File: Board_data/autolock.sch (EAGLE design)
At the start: 10 parts, among them CN1 RASPBERRYPI-GPIO

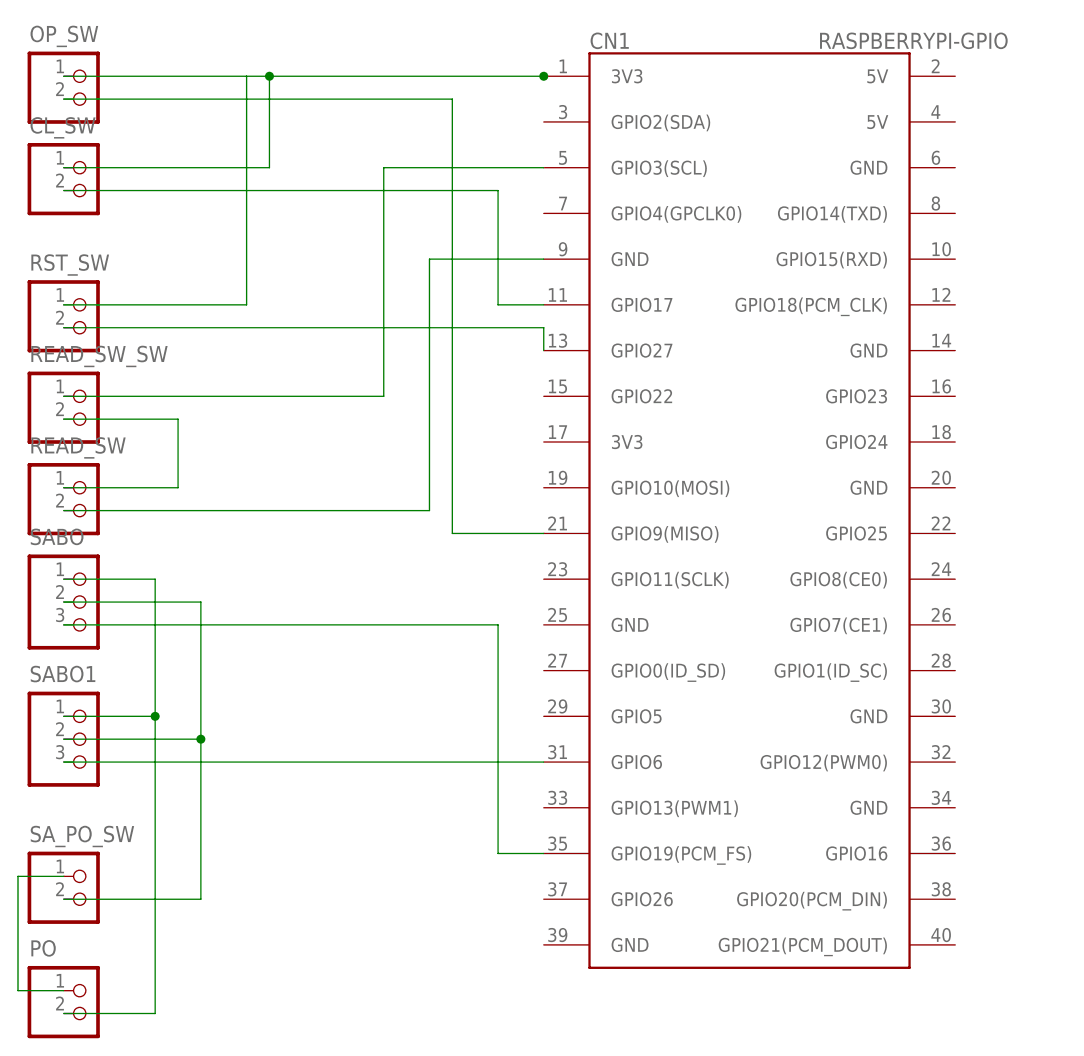
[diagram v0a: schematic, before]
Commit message: 基板修正・リードスイッチ調整
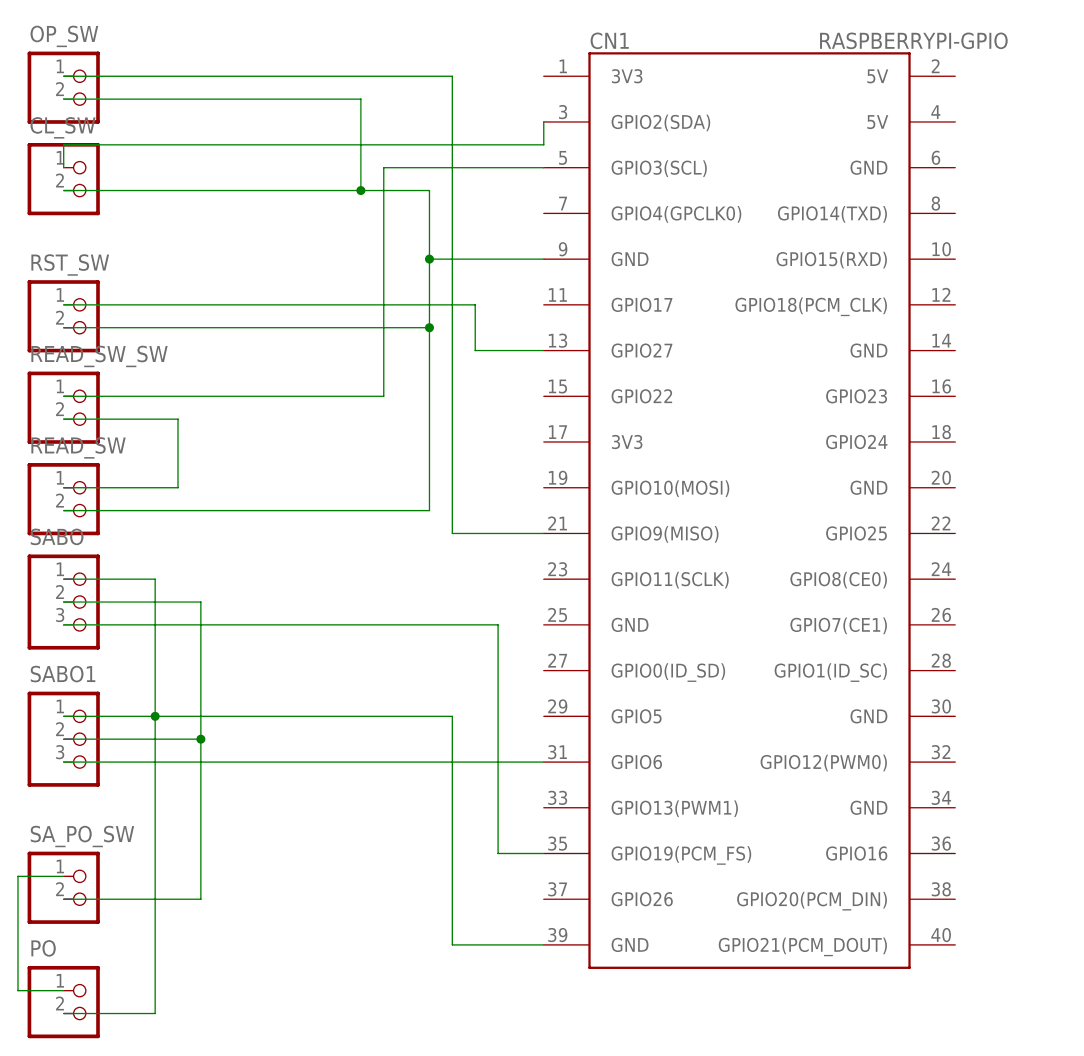
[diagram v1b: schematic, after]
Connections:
- removed net N$12: PO.2, SABO.1, SABO1.1
- removed net N$4: CN1.GND@2, READ_SW.2
- removed net N$8: CL_SW.2, CN1.GPIO17
- removed net N$9: CN1.GPIO27, RST_SW.2
- new net GND: CL_SW.2, CN1.GND@2, CN1.GND@8, OP_SW.2, PO.2, READ_SW.2, RST_SW.2, SABO.1, SABO1.1
- new net N$14: CN1.GPIO27, RST_SW.1
- net N$1: now also CN1.GPIO9(MISO); no longer CL_SW.1, CN1.3V3@1, RST_SW.1
- net N$2: now also CL_SW.1, CN1.GPIO2(SDA); no longer CN1.GPIO9(MISO), OP_SW.2
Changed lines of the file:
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@@
 <segment>
 <pinref part="OP_SW" gate="G$1" pin="1"/>
-<pinref part="CN1" gate="G$1" pin="3V3@1"/>
-<wire x1="30.48" y1="93.98" x2="50.8" y2="93.98" width="0.1524" layer="91"/>
-<pinref part="RST_SW" gate="G$1" pin="1"/>
-<wire x1="30.48" y1="68.58" x2="50.8" y2="68.58" width="0.1524" layer="91"/>
-<wire x1="50.8" y1="68.58" x2="50.8" y2="93.98" width="0.1524" layer="91"/>
-<wire x1="50.8" y1="93.98" x2="53.34" y2="93.98" width="0.1524" layer="91"/>
-<junction x="83.82" y="93.98"/>
-<pinref part="CL_SW" gate="G$1" pin="1"/>
-<wire x1="53.34" y1="93.98" x2="83.82" y2="93.98" width="0.1524" layer="91"/>
-<wire x1="30.48" y1="83.82" x2="53.34" y2="83.82" width="0.1524" layer="91"/>
-<wire x1="53.34" y1="83.82" x2="53.34" y2="93.98" width="0.1524" layer="91"/>
-<junction x="53.34" y="93.98"/>
-</segment>
-</net>
-<net name="N$2" class="0">
-<segment>
-<pinref part="OP_SW" gate="G$1" pin="2"/>
-<wire x1="30.48" y1="91.44" x2="73.66" y2="91.44" width="0.1524" layer="91"/>
-<wire x1="73.66" y1="91.44" x2="73.66" y2="43.18" width="0.1524" layer="91"/>
+<wire x1="30.48" y1="93.98" x2="73.66" y2="93.98" width="0.1524" layer="91"/>
+<wire x1="73.66" y1="93.98" x2="73.66" y2="43.18" width="0.1524" layer="91"/>
 <pinref part="CN1" gate="G$1" pin="GPIO9(MISO)"/>
 <wire x1="73.66" y1="43.18" x2="83.82" y2="43.18" width="0.1524" layer="91"/>
@@
 </segment>
 </net>
-<net name="N$4" class="0">
+<net name="GND" class="0">
 <segment>
-<wire x1="71.12" y1="45.72" x2="71.12" y2="73.66" width="0.1524" layer="91"/>
+<wire x1="71.12" y1="45.72" x2="71.12" y2="66.04" width="0.1524" layer="91"/>
 <pinref part="CN1" gate="G$1" pin="GND@2"/>
+<wire x1="71.12" y1="66.04" x2="71.12" y2="73.66" width="0.1524" layer="91"/>
 <wire x1="71.12" y1="73.66" x2="83.82" y2="73.66" width="0.1524" layer="91"/>
 <pinref part="READ_SW" gate="G$1" pin="2"/>
 <wire x1="30.48" y1="45.72" x2="71.12" y2="45.72" width="0.1524" layer="91"/>
+<pinref part="CL_SW" gate="G$1" pin="2"/>
+<wire x1="30.48" y1="81.28" x2="63.5" y2="81.28" width="0.1524" layer="91"/>
+<wire x1="63.5" y1="81.28" x2="71.12" y2="81.28" width="0.1524" layer="91"/>
+<wire x1="71.12" y1="81.28" x2="71.12" y2="73.66" width="0.1524" layer="91"/>
+<junction x="71.12" y="73.66"/>
+<pinref part="OP_SW" gate="G$1" pin="2"/>
+<wire x1="30.48" y1="91.44" x2="63.5" y2="91.44" width="0.1524" layer="91"/>
+<wire x1="63.5" y1="91.44" x2="63.5" y2="81.28" width="0.1524" layer="91"/>
+<junction x="63.5" y="81.28"/>
+<pinref part="RST_SW" gate="G$1" pin="2"/>
+<wire x1="30.48" y1="66.04" x2="71.12" y2="66.04" width="0.1524" layer="91"/>
+<junction x="71.12" y="66.04"/>
+</segment>
+<segment>
+<pinref part="SABO" gate="G$1" pin="1"/>
+<wire x1="30.48" y1="38.1" x2="40.64" y2="38.1" width="0.1524" layer="91"/>
+<wire x1="40.64" y1="38.1" x2="40.64" y2="22.86" width="0.1524" layer="91"/>
+<wire x1="40.64" y1="22.86" x2="40.64" y2="-10.16" width="0.1524" layer="91"/>
+<pinref part="SABO1" gate="G$1" pin="1"/>
+<wire x1="30.48" y1="22.86" x2="40.64" y2="22.86" width="0.1524" layer="91"/>
+<junction x="40.64" y="22.86"/>
+<wire x1="30.48" y1="-10.16" x2="40.64" y2="-10.16" width="0.1524" layer="91"/>
+<pinref part="PO" gate="G$1" pin="2"/>
+<wire x1="40.64" y1="22.86" x2="73.66" y2="22.86" width="0.1524" layer="91"/>
+<pinref part="CN1" gate="G$1" pin="GND@8"/>
+<wire x1="73.66" y1="-2.54" x2="83.82" y2="-2.54" width="0.1524" layer="91"/>
+<wire x1="73.66" y1="22.86" x2="73.66" y2="-2.54" width="0.1524" layer="91"/>
 </segment>
 </net>
@@
 <pinref part="SABO" gate="G$1" pin="3"/>
 <wire x1="30.48" y1="33.02" x2="78.74" y2="33.02" width="0.1524" layer="91"/>
-</segment>
-</net>
-<net name="N$9" class="0">
-<segment>
-<pinref part="RST_SW" gate="G$1" pin="2"/>
-<pinref part="CN1" gate="G$1" pin="GPIO27"/>
-<wire x1="30.48" y1="66.04" x2="83.82" y2="66.04" width="0.1524" layer="91"/>
-<wire x1="83.82" y1="66.04" x2="83.82" y2="63.5" width="0.1524" layer="91"/>
 </segment>
 </net>
@@
 </segment>
 </net>
-<net name="N$8" class="0">
-<segment>
-<pinref part="CL_SW" gate="G$1" pin="2"/>
-<wire x1="30.48" y1="81.28" x2="78.74" y2="81.28" width="0.1524" layer="91"/>
-<wire x1="78.74" y1="81.28" x2="78.74" y2="68.58" width="0.1524" layer="91"/>
-<pinref part="CN1" gate="G$1" pin="GPIO17"/>
-<wire x1="78.74" y1="68.58" x2="83.82" y2="68.58" width="0.1524" layer="91"/>
-</segment>
-</net>
 <net name="N$10" class="0">
 <segment>
@@
 <pinref part="CN1" gate="G$1" pin="GPIO6"/>
 <wire x1="30.48" y1="17.78" x2="83.82" y2="17.78" width="0.1524" layer="91"/>
-</segment>
-</net>
-<net name="N$12" class="0">
-<segment>
-<pinref part="SABO" gate="G$1" pin="1"/>
-<wire x1="30.48" y1="38.1" x2="40.64" y2="38.1" width="0.1524" layer="91"/>
-<wire x1="40.64" y1="38.1" x2="40.64" y2="22.86" width="0.1524" layer="91"/>
-<wire x1="40.64" y1="22.86" x2="40.64" y2="-10.16" width="0.1524" layer="91"/>
-<pinref part="SABO1" gate="G$1" pin="1"/>
-<wire x1="30.48" y1="22.86" x2="40.64" y2="22.86" width="0.1524" layer="91"/>
-<junction x="40.64" y="22.86"/>
-<wire x1="30.48" y1="-10.16" x2="40.64" y2="-10.16" width="0.1524" layer="91"/>
-<pinref part="PO" gate="G$1" pin="2"/>
 </segment>
 </net>
@@
 </segment>
 </net>
+<net name="N$14" class="0">
+<segment>
+<pinref part="RST_SW" gate="G$1" pin="1"/>
+<wire x1="30.48" y1="68.58" x2="76.2" y2="68.58" width="0.1524" layer="91"/>
+<pinref part="CN1" gate="G$1" pin="GPIO27"/>
+<wire x1="76.2" y1="68.58" x2="76.2" y2="63.5" width="0.1524" layer="91"/>
+<wire x1="76.2" y1="63.5" x2="83.82" y2="63.5" width="0.1524" layer="91"/>
+</segment>
+</net>
+<net name="N$2" class="0">
+<segment>
+<pinref part="CL_SW" gate="G$1" pin="1"/>
+<wire x1="30.48" y1="83.82" x2="30.48" y2="86.36" width="0.1524" layer="91"/>
+<wire x1="30.48" y1="86.36" x2="83.82" y2="86.36" width="0.1524" layer="91"/>
+<pinref part="CN1" gate="G$1" pin="GPIO2(SDA)"/>
+<wire x1="83.82" y1="86.36" x2="83.82" y2="88.9" width="0.1524" layer="91"/>
+</segment>
+</net>
